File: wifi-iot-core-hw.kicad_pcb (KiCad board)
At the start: 2 copper layers, 34.3 x 61 mm, 49 parts, among them P1 USB, P10 CONN_01X01, P11 CONN_01X01, P3 CONN_01X16, P4 CONN_01X04, P5 CONN_01X16, P6 CONN_01X03, P7 CONN_01X03, P8 CONN_01X01, P9 CONN_01X01, U1 LP2985LV, U2 STM32F103C8Tx, U3 ESP-07v2, Y1 8MHz

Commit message: Fix Schematic & PCB
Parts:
- removed D1: Led PWR, LEDs:LED_0805
- removed G***: logo5_silkscreen-front_5mm, logo:logo5_silkscreen-front_5mm
- removed P5: CONN_01X16, Pin_Headers:Pin_Header_Straight_1x16
- removed P6, P7: CONN_01X03, Pin_Headers:Pin_Header_Straight_1x03
- removed PA15: SW_PUSH_SMALL_H, Buttons_Switches_SMD:SW_SPST_B3U-1000P-B
- removed the RST at (113.4, 133.5)
- added A15: SW_PUSH_SMALL_H, lib:SW_SPST_B3U-1000P-B, F.Cu at (131.6, 133.1)
- added C18: 100nF, lib:C_0603, F.Cu at (127.3, 102.0)
- added C19: 15pF, lib:C_0603, F.Cu at (114.0, 104.5)
- added C20: 15pf, lib:C_0603, F.Cu at (114.0, 111.3)
- added P2: CONN_01X20, Pin_Headers:Pin_Header_Straight_1x20, F.Cu at (109.2, 81.3)
- added PB1: Led PWR, LEDs:LED_0805, F.Cu at (129.8, 129.1)
- added RST: RST, lib:SW_SPST_B3U-1000P-B, F.Cu at (114.8, 133.1)
- added VAL**: oshw_logo_500, lib:logo5, F.Cu at (123.2, 121.3)
- added Y2: 32.687, lib:crystal_smd_32.768_2Pin, F.Cu at (113.7, 107.9)
- C1, C10, C11, C12, C13, C14, C15, C16, C5, C6, C7, C8, C9: footprint Capacitors_SMD:C_0603 -> lib:C_0603
- C3: value 1uF -> 10nF; footprint Capacitors_SMD:C_0603 -> lib:C_0603
- P1: footprint w_conn_pc:conn_usb_B_micro_smd-2 -> lib:Micro_usb_B_smd
- P10, P11, P8, P9: footprint Mounting_Holes:MountingHole_3.5mm -> lib:MountingHole_2mm
- P3: value CONN_01X16 -> CONN_01X20; footprint Pin_Headers:Pin_Header_Straight_1x16 -> Pin_Headers:Pin_Header_Straight_1x20
- R1, R10, R11, R12, R13, R2, R3, R4, R5, R6, R7, R8, R9: footprint Resistors_SMD:R_0603 -> lib:R_0603
- U2: footprint Housings_QFP:LQFP-48_7x7mm_Pitch0.5mm -> lib:LQFP-48_Pin1.7x0.3mm_Pitch0.5mm
- U3: footprint ESP8266:ESP-07v2-smd-16pin -> lib:ESP-07v2-smd-16pin
- Y1: footprint Crystal:HC49_sm -> lib:Crystal_SMD_5032_4Pads
- moved C11 37.7 mm to (126.8, 126.5)
- moved C16 33.3 mm to (129.1, 125.7), turned to 0 degrees
- moved P10 29.7 mm to (137.2, 132.8)
- moved C12 27.4 mm to (132.7, 122.8)
- moved P11 27.3 mm to (109.2, 132.8)
- moved C15 21.1 mm to (116.0, 102.0)
- moved C9 20.6 mm to (128.9, 102.0), turned to 270 degrees
- moved Y1 19.9 mm to (120.0, 102.0), turned to 180 degrees
- moved R13 19.8 mm to (113.0, 85.8)
- moved C14 18.9 mm to (124.0, 102.0), turned to 270 degrees
- moved C10 18.1 mm to (130.6, 102.0), turned to 270 degrees
- moved C7 15.8 mm to (113.8, 128.0), turned to 0 degrees
- moved P3 10.2 mm to (137.2, 81.3)
- moved R8 9.39 mm to (125.7, 102.0)
- moved R11 8.81 mm to (133.3, 88.8), turned to 90 degrees
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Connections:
- net /OSC_IN renamed Net-(C14-Pad1)
- net /OSC_OUT renamed Net-(C15-Pad1)
- P3 pad 10: PB15 -> PB5
- P3 pad 11: PB14 -> PB4
- P3 pad 12: PB13 -> PB3
- P3 pad 13: PB12 -> PA8
- P3 pad 14: PB10 -> PB15
- P3 pad 15: GNDREF -> PB14
- P3 pad 16: +3V3 -> PB13
- P3 pad 3: PB9 -> /ESP_TXD
- P3 pad 4: PB8 -> /ESP_RXD
- P3 pad 5: PB5 -> /PRO
- P3 pad 6: PB4 -> PB9
- P3 pad 7: PB3 -> PB8
- P3 pad 8: PA9 -> PB7
- P3 pad 9: PA8 -> PB6
- R13 pad 2: ESP_PRO -> /PRO
- U2 pad 18: ESP_PRO -> /PRO
- U2 pad 2: PA13 -> /USB_DIS
- U2 pad 3: PA14 -> Net-(C19-Pad1)
- U2 pad 30: PA9 -> /ESP_RXD
- U2 pad 31: /USB_DIS -> /ESP_TXD
- U2 pad 4: PA15 -> Net-(C20-Pad1)
- U2 pad 42: RXD -> PB6
- U2 pad 43: TXD -> PB7
- U3 pad 12: ESP_PRO -> /PRO
- U3 pad 15: RXD -> /ESP_RXD
- U3 pad 16: TXD -> /ESP_TXD
- U3 pad 5: Net-(P6-Pad3) -> GPIO14
- U3 pad 6: Net-(P6-Pad2) -> GPIO12
- U3 pad 7: Net-(P6-Pad1) -> GPIO13
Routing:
- net +3V3: track 173.3 -> 80.3 mm, vias 17 -> 0
- net ESP_PRO: track 50.3 -> 0.00 mm, vias 2 -> 0
- net /NRST: track 93.4 -> 44.4 mm, vias 7 -> 4
- net /ESP_TXD: track 0.00 -> 48.7 mm, vias 0 -> 5
- net /ESP_RXD: track 0.00 -> 45.5 mm, vias 0 -> 2
- net TXD: track 44.9 -> 0.00 mm, vias 2 -> 0
- net RXD: track 44.8 -> 0.00 mm, vias 2 -> 0
- net GNDREF: track 172.4 -> 203.9 mm, vias 6 -> 8
- net /PRO: track 0.00 -> 30.2 mm
- net PA13: track 21.2 -> 0.00 mm
- net PA14: track 19.6 -> 0.00 mm
- net PB10: track 35.8 -> 16.9 mm, vias 2 -> 1
- net /SWDIO: track 23.5 -> 5.61 mm, vias 2 -> 0
- net PA15: track 17.4 -> 0.00 mm
- net PB7: track 0.00 -> 17.4 mm
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- removed copper zone on B.Cu, net GNDREF
- removed copper zone on F.Cu, net GNDREF
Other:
- board size 34.3 x 61 mm -> 33 x 58.4 mm
- net class Default: trace_width 0.4 -> 0.35; via_dia 0.8 -> 1.2; via_drill 0.4 -> 0.7
- rule trace_min: 0.25 -> 0.3
- rule via_min_drill: 0.3 -> 0.7
- rule via_min_size: 0.8 -> 1.2
- board text added: "A15"
- board text added: "GPIO12"
- board text added: "GPIO13"
- board text added: "GPIO14"
- board text added: "PB3"
- board text added: "PB6"
- board text added: "PB7"
- board text added: "PB9"
- board text added: "PRO"
- board text added: "VBAT"
- board text removed: "3,3V"
- board text removed: "3.3v"
- board text removed: "ESP_PRO"
- board text removed: "GP12"
- board text removed: "GP13"
- board text removed: "GP14"
- board text removed: "PA9"
- board text removed: "PB0"
- board text removed: "PB11"
- board text removed: "PC13"
- board text removed: "PC14"
- board text removed: "PC15"
- board text removed: "SWCLK"
- board text removed: "SWDIO"

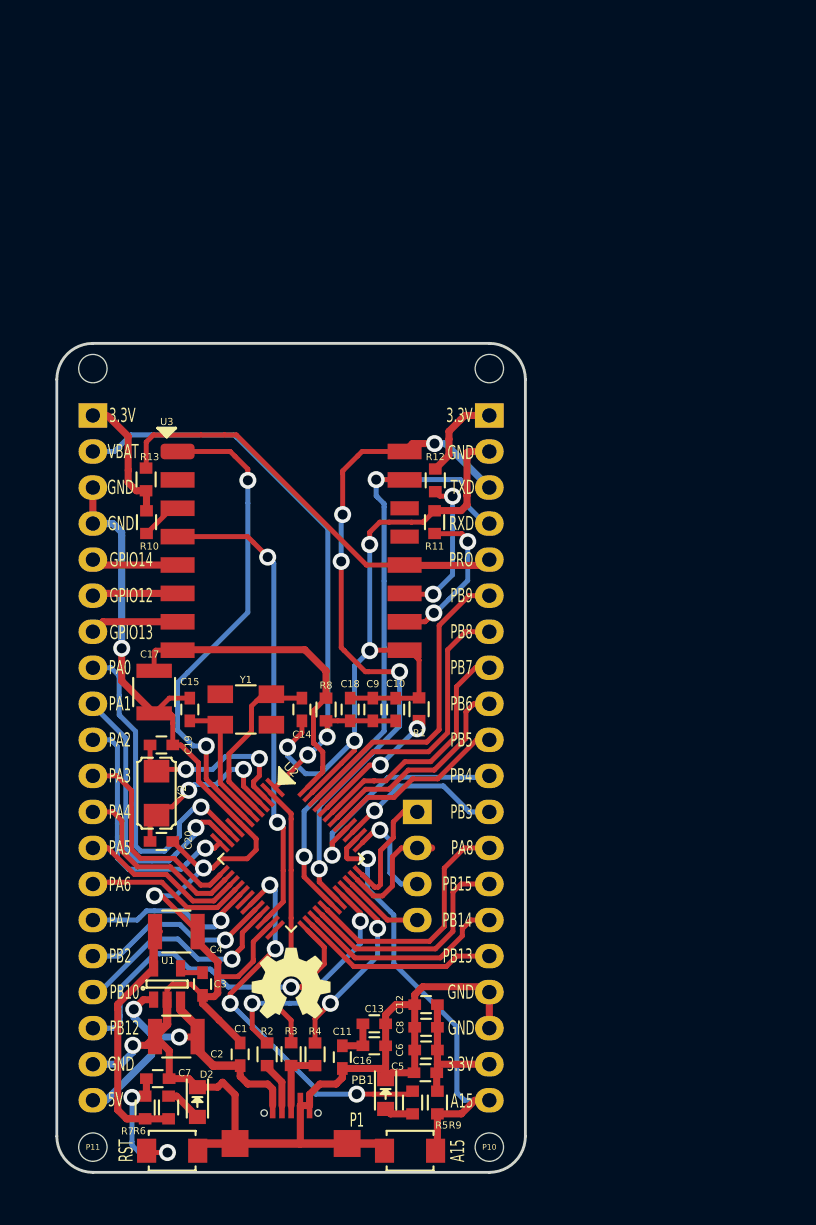
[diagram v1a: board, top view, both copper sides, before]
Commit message: resolve #10
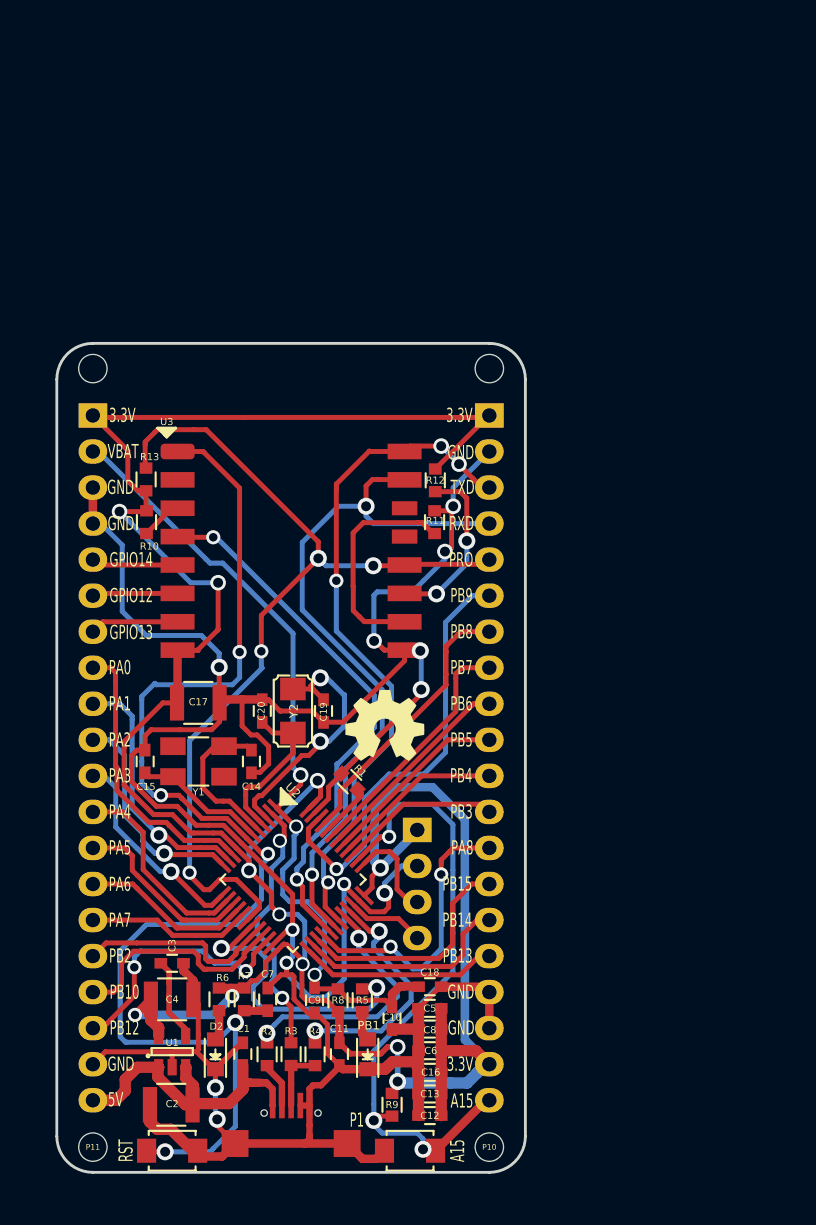
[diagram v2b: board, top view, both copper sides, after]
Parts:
- moved C10 21.8 mm to (130.3, 123.8), turned to 90 degrees
- moved C9 20.9 mm to (124.8, 122.5), turned to 90 degrees
- moved R8 20.5 mm to (126.5, 122.5), turned to 270 degrees
- moved C18 20.3 mm to (133.0, 121.5), turned to 180 degrees
- moved VAL** 19.3 mm to (129.8, 103.1)
- moved C19 11.7 mm to (125.5, 102.1), turned to 270 degrees
- moved C20 11.6 mm to (121.2, 102.1), turned to 90 degrees
- moved Y2 11.2 mm to (123.3, 102.1)
- moved R7 10.3 mm to (119.9, 122.4), turned to 90 degrees
- moved C7 9.55 mm to (121.5, 122.4), turned to 90 degrees
- moved R6 8.41 mm to (118.1, 122.4), turned to 270 degrees
- moved R5 8.03 mm to (128.2, 122.5)
- moved C12 7.82 mm to (133.0, 130.6)
- moved R1 7.08 mm to (127.3, 107.1), turned to 135 degrees
- moved C13 6.31 mm to (133.0, 129.1), turned to 180 degrees
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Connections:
- C18 pad 1: /VBAT -> GNDREF
- C18 pad 2: GNDREF -> /VBAT
- P2 pad 18: PB12 -> PB11
- P3 pad 13: PA8 -> PB15
- P3 pad 14: PB15 -> PB14
- P3 pad 15: PB14 -> PB13
- P3 pad 16: PB13 -> PB12
- U2 pad 22: GPIO16 -> PB11
- U2 pad 29: PA8 -> GPIO16
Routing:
- net +3V3: track 80.3 -> 195.4 mm, vias 0 -> 11
- net /NRST: track 44.4 -> 90.3 mm, vias 4 -> 5
- net /PRO: track 30.2 -> 65.5 mm, vias 0 -> 4
- net GNDREF: track 203.9 -> 226.4 mm, vias 8 -> 12
- net PB11: track 0.00 -> 18.0 mm, vias 0 -> 2
- net PA8: track 17.5 -> 0.00 mm
- net /BUTTON: track 31.5 -> 45.4 mm, vias 1 -> 3
- net /VBAT: track 45.7 -> 57.6 mm, vias 2 -> 4
- net PB12: track 24.4 -> 14.0 mm, vias 1 -> 0
- net PB9: track 22.3 -> 30.8 mm, vias 0 -> 1
- net Led_u: track 27.6 -> 20.8 mm, vias 4 -> 2
- net /ESP_RXD: track 45.5 -> 51.5 mm
- net Net-(C19-Pad1): track 13.2 -> 18.8 mm
- net Net-(R1-Pad1): track 9.27 -> 3.78 mm, vias 2 -> 0
- net GPIO16: track 33.5 -> 38.4 mm
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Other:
- net class Default: via_dia 1.2 -> 1
- rule via_min_drill: 0.7 -> 0.6
- rule via_min_size: 1.2 -> 1

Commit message: Fix schematic & PCB
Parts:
- removed A15: SW_PUSH_SMALL_H, lib:SW_SPST_B3U-1000P-B
- removed P10, P11, P9: CONN_01X01, lib:MountingHole_2mm
- removed PB1: Led PWR, LEDs:LED_0805
- removed RST: RST, lib:SW_SPST_B3U-1000P-B
- added C21: 10nF, lib:C_0603, F.Cu at (117.1, 126.7)
- added D1: Led GPIO16, LEDs:LED_0805, F.Cu at (125.9, 123.9)
- added P5: CONN_01X01, lib:MountingHole_2.5mm, F.Cu at (109.5, 132.8)
- added P6: CONN_01X01, lib:MountingHole_2.5mm, F.Cu at (109.5, 78.0)
- added P7: CONN_01X04, Pin_Headers:Pin_Header_Straight_1x04, F.Cu at (130.7, 111.4)
- added SW1: RST, lib:SW_SPST_B3U-1000P-B, F.Cu at (114.6, 132.6)
- added SW2: SW_PUSH_SMALL_H, lib:SW_SPST_B3U-1000P-B, F.Cu at (129.3, 132.6)
- C13: value 0.1uF -> 10uF-50v; footprint lib:C_0603 -> Capacitors_SMD:C_1210
- C14: value 10pF -> 10uF-50v; footprint lib:C_0603 -> Capacitors_SMD:C_1210
- C15: value 10pF -> 0.1uF
- C16: value 0.1uF -> 1uF
- C17: value 10uF-50v -> 0.1uF; footprint Capacitors_SMD:C_1210 -> lib:C_0603
- C18: value 100nF -> 1uF
- C19: value 15pF -> 0.1uF
- C20: value 15pf -> 0.1uF
- C3: value 10nF -> 100nF
- C4: value 10uF-50v -> 10pF; footprint Capacitors_SMD:C_1210 -> lib:C_0603
- C5: value 0.1uF -> 10pF
- C6: value 1uF -> 15pF
- C7: value 0.1uF -> 15pf
- C8: value 0.1uF -> 470pF
- C9: value 1uF -> 0.1uF
- P1: value USB -> CONN_01X20; footprint lib:Micro_usb_B_smd -> Pin_Headers:Pin_Header_Straight_1x20
- P3: value CONN_01X20 -> CONN_01X01; footprint Pin_Headers:Pin_Header_Straight_1x20 -> lib:MountingHole_2.5mm
- P4: value CONN_01X04 -> CONN_01X01; footprint Pin_Headers:Pin_Header_Straight_1x04 -> lib:MountingHole_2.5mm
- P8: value CONN_01X01 -> USB; footprint lib:MountingHole_2mm -> lib:Micro_usb_B_smd
- R10: value 10K -> 1.5K
- R11, R12: value 10K -> 22
- R13, R7: value 10K -> 10k
- R2, R4: value 22 -> 10K
- R3: value 1.5K -> 10K
- R5: value 10k -> 10K
- R8: value 0R -> 10k
- R9: value 10K -> 0R
- U1: value LP2985LV -> ESP-07v2; footprint TO_SOT_Packages_SMD:SOT-23-5 -> lib:ESP-07v2-smd-16pin
- U3: value ESP-07v2 -> LP2985LV; footprint lib:ESP-07v2-smd-16pin -> TO_SOT_Packages_SMD:SOT-23-5
- moved P8 56.1 mm to (121.9, 132.6)
- moved P1 53.2 mm to (109.2, 81.3)
- moved R7 43.4 mm to (130.8, 80.4)
- moved U1 43.2 mm to (113.9, 82.9), turned to 0 degrees
- moved R12 42.9 mm to (120.3, 126.7)
- moved R6 42.3 mm to (112.9, 80.4), turned to 90 degrees
- moved U3 41.9 mm to (114.1, 125.7), turned to 90 degrees
- moved R11 39.2 mm to (123.5, 126.7), turned to 270 degrees
- moved R10 39.0 mm to (121.9, 126.7), turned to 270 degrees
- moved C12 37.1 mm to (113.0, 99.3), turned to 180 degrees
- moved R13 36.0 mm to (117.2, 121.6), turned to 270 degrees
- moved C15 28.4 mm to (129.8, 128.5), turned to 0 degrees
- moved C17 27.0 mm to (129.8, 125.1)
- moved R2 26.9 mm to (119.8, 99.5), turned to 0 degrees
- moved R3 26.8 mm to (123.3, 99.5), turned to 0 degrees
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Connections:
- C1 pad 1: +5V -> +3V3
- C10 pad 2: /VBAT -> +3V3
- C12 pad 1: GNDREF -> +3V3
- C12 pad 2: +3V3 -> GNDREF
- C13 pad 1: +3V3 -> +5V
- C14 pad 1: Net-(C14-Pad1) -> +3V3
- C15 pad 1: Net-(C15-Pad1) -> GNDREF
- C15 pad 2: GNDREF -> +3V3
- C16 pad 1: +3V3 -> GNDREF
- C16 pad 2: GNDREF -> +3V3
- C17 pad 1: +3V3 -> GNDREF
- C17 pad 2: GNDREF -> +3V3
- C19 pad 1: Net-(C19-Pad1) -> GNDREF
- C19 pad 2: GNDREF -> /VBAT
- C2 pad 1: +5V -> +3V3
- C20 pad 1: Net-(C20-Pad1) -> +5V
- C3 pad 1: Net-(C3-Pad1) -> GNDREF
- C3 pad 2: GNDREF -> /VBAT
- C4 pad 1: +3V3 -> Net-(C4-Pad1)
- C5 pad 1: GNDREF -> Net-(C5-Pad1)
- C5 pad 2: +3V3 -> GNDREF
- C6 pad 1: GNDREF -> Net-(C6-Pad1)
- C6 pad 2: +3V3 -> GNDREF
- C7 pad 1: /NRST -> Net-(C7-Pad1)
- C8 pad 1: GNDREF -> /ESP_PRO
- C8 pad 2: +3V3 -> GNDREF
- C9 pad 1: GNDREF -> /RST
- C9 pad 2: /VBAT -> GNDREF
- P1 pad 1: +5V -> +3V3
- P1 pad 2: Net-(P1-Pad2) -> /VBAT
- P1 pad 3: Net-(P1-Pad3) -> GNDREF
- P1 pad 5: GNDREF -> GPIO14
- P2 pad 10: PA2 -> PB5
- P2 pad 11: PA3 -> PB4
- P2 pad 12: PA4 -> PB3
- P2 pad 13: PA5 -> PB15
- P2 pad 14: PA6 -> PB14
- P2 pad 15: PA7 -> PB13
- P2 pad 16: PB2 -> PB12
- P2 pad 17: PB10 -> GNDREF
- P2 pad 18: PB11 -> GNDREF
- P2 pad 19: GNDREF -> +3V3
- P2 pad 2: /VBAT -> GNDREF
- P2 pad 20: +5V -> +3V3
- P2 pad 3: GNDREF -> /ESP_TXD
- P2 pad 4: GNDREF -> /ESP_RXD
- P2 pad 5: GPIO14 -> /ESP_PRO
- P2 pad 6: GPIO12 -> PB9
- P2 pad 7: GPIO13 -> PB8
- P2 pad 8: PA0 -> PB7
- P2 pad 9: PA1 -> PB6
- R10 pad 1: Net-(R10-Pad1) -> /USB_DIS
- R10 pad 2: +3V3 -> Net-(P8-Pad3)
- R11 pad 1: Net-(R11-Pad1) -> /USB_DP
- R11 pad 2: GNDREF -> Net-(P8-Pad3)
- R12 pad 1: +3V3 -> /USB_DM
- R12 pad 2: Net-(R12-Pad2) -> Net-(P8-Pad2)
- R13 pad 2: /PRO -> Net-(D2-Pad2)
- R2 pad 1: /USB_DM -> +3V3
- R2 pad 2: Net-(P1-Pad2) -> Net-(R2-Pad2)
- R3 pad 1: /USB_DIS -> Net-(R3-Pad1)
- R3 pad 2: Net-(P1-Pad3) -> GNDREF
- R4 pad 1: /USB_DP -> /RST
- R4 pad 2: Net-(P1-Pad3) -> +3V3
- R5 pad 1: Led_u -> /ESP_PRO
- R5 pad 2: Net-(D1-Pad2) -> +3V3
- R6 pad 2: Net-(D2-Pad2) -> /CH_PD
- R7 pad 1: /NRST -> +3V3
- R7 pad 2: +3V3 -> /ESP_PRO
- R8 pad 1: /VBAT -> +3V3
- R8 pad 2: +3V3 -> Net-(D1-Pad2)
- R9 pad 1: /BUTTON -> /VBAT
- U1 pad 1: +5V -> /ESP_RST
- U1 pad 2: GNDREF -> Net-(U1-Pad2)
- U1 pad 3: +5V -> /CH_PD
- U1 pad 4: Net-(C3-Pad1) -> /GPIO16
- U1 pad 5: +3V3 -> GPIO14
- U2 pad 18: /PRO -> /ESP_RST
- U2 pad 19: Led_u -> /CH_PD
- U2 pad 29: GPIO16 -> /GPIO16
- U2 pad 3: Net-(C19-Pad1) -> Net-(C6-Pad1)
- U2 pad 38: /BUTTON -> /ESP_PRO
- U2 pad 4: Net-(C20-Pad1) -> Net-(C7-Pad1)
- U2 pad 5: Net-(C14-Pad1) -> Net-(C4-Pad1)
- U2 pad 6: Net-(C15-Pad1) -> Net-(C5-Pad1)
- U2 pad 7: /NRST -> /RST
- U3 pad 1: /NRST -> +5V
- U3 pad 2: Net-(U3-Pad2) -> GNDREF
- U3 pad 3: Net-(R10-Pad1) -> +5V
- U3 pad 4: GPIO16 -> Net-(C21-Pad1)
- U3 pad 5: GPIO14 -> +3V3
- Y1 pad 1: Net-(C14-Pad1) -> Net-(C4-Pad1)
- Y1 pad 2: Net-(C15-Pad1) -> Net-(C5-Pad1)
- Y2 pad 1: Net-(C19-Pad1) -> Net-(C6-Pad1)
- Y2 pad 2: Net-(C20-Pad1) -> Net-(C7-Pad1)
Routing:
- net /NRST: track 90.3 -> 0.00 mm, vias 5 -> 0
- net /ESP_PRO: track 0.00 -> 86.6 mm, vias 0 -> 3
- net /PRO: track 65.5 -> 0.00 mm, vias 4 -> 0
- net /GPIO16: track 0.00 -> 54.8 mm, vias 0 -> 3
- net /CH_PD: track 0.00 -> 52.3 mm, vias 0 -> 2
- net /RST: track 0.00 -> 45.6 mm, vias 0 -> 4
- net /BUTTON: track 45.4 -> 0.00 mm, vias 3 -> 0
- net /ESP_RST: track 0.00 -> 44.9 mm, vias 0 -> 2
- net GPIO16: track 38.4 -> 0.00 mm, vias 2 -> 0
- net /VBAT: track 57.6 -> 80.9 mm
- net Led_u: track 20.8 -> 0.00 mm, vias 2 -> 0
- net Net-(C19-Pad1): track 18.8 -> 0.00 mm, vias 2 -> 0
- net Net-(R11-Pad1): track 15.8 -> 0.00 mm
- net Net-(R1-Pad1): track 3.78 -> 19.3 mm
- net Net-(R2-Pad2): track 0.00 -> 15.0 mm
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- added copper zone on B.Cu, net GNDREF
- added copper zone on F.Cu, net GNDREF
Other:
- board size 33 x 58.4 mm -> 28.4 x 58.4 mm
- net class Default: trace_width 0.35 -> 0.33; via_dia 1 -> 1.1; via_drill 0.7 -> 0.6
- rule trace_min: 0.3 -> 0.33
- rule via_min_size: 1 -> 1.1
- board text added: "1p.io/wic"
- board text added: "3.3v"
- board text added: "5v"
- board text added: "IO12"
- board text added: "IO13"
- board text added: "IO14"
- board text added: "PB11"
- board text added: "SWCLK"
- board text added: "SWDIO"
- board text removed: "5V"
- board text removed: "A15"
- board text removed: "GPIO12"
- board text removed: "GPIO13"
- board text removed: "GPIO14"
- board text removed: "PA8"
